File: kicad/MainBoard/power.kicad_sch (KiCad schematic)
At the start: 75 parts, among them J16 Conn_01x02_Female, J20 USB_C_Receptacle, Q16 AO3401A, Q17 AO3400A, SW1 SW_SPDT, U13 BQ27441-G1, U14 HY2111-GB, U15 FS8205A, U17 TPS61088, U2 BQ25601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

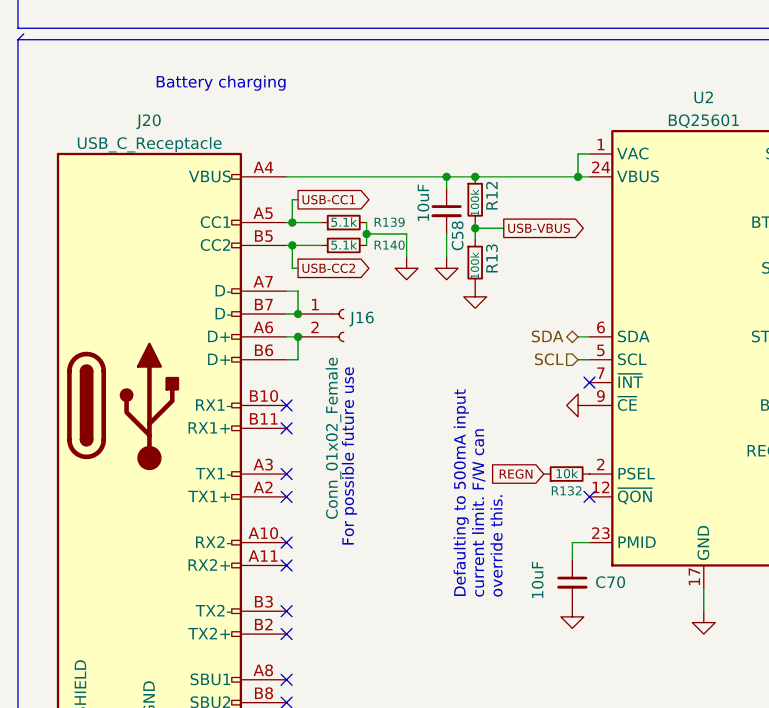
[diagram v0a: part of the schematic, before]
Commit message: v2.6 schematic + pcb changes
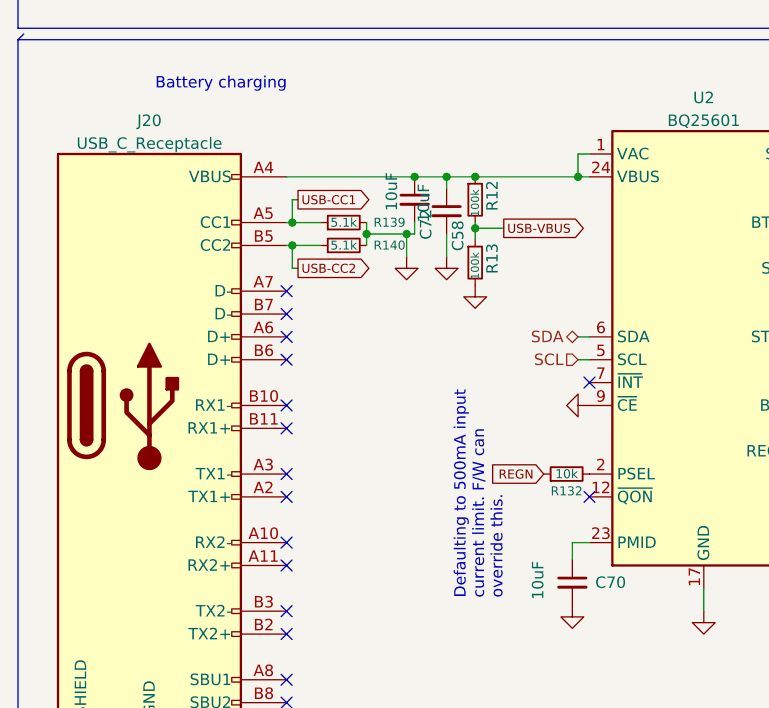
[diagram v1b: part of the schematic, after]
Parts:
- removed J16: Conn_01x02_Female, Connector_PinSocket_2.54mm:PinSocket_1x02_P2.54mm_Vertical, symbol Connector:Conn_01x02_Female
- added C72: 10uF, Capacitor_SMD:C_0603_1608Metric_Pad1.08x0.95mm_HandSolder, symbol Device:C_Small
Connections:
- net GND: now also C72.2
- net at J20.A7 (D-): no longer J20.B7 (D-)
- net at J20.A6 (D+): no longer J20.B6 (D+)
- net at C58.1, J20.A4 (VBUS), J20.A9 (VBUS)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: now also C72.1
- no-connect marks 14 -> 18
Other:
- note removed: "For possible future use"
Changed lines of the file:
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@@
   (junction (at 100.33 191.77) (diameter 0) (color 0 0 0 0)
   )
-  (junction (at 44.45 113.665) (diameter 0) (color 0 0 0 0)
-  )
   (junction (at 113.665 191.77) (diameter 0) (color 0 0 0 0)
   )
@@
   (junction (at 135.255 22.86) (diameter 0) (color 0 0 0 0)
   )
+  (junction (at 56.515 104.775) (diameter 0) (color 0 0 0 0)
+  )
   (junction (at 32.385 191.77) (diameter 0) (color 0 0 0 0)
   )
@@
   (junction (at 90.805 22.86) (diameter 0) (color 0 0 0 0)
   )
-  (junction (at 44.45 116.205) (diameter 0) (color 0 0 0 0)
-  )
   (junction (at 64.135 98.425) (diameter 0) (color 0 0 0 0)
   )
@@
   (junction (at 103.505 118.745) (diameter 0) (color 0 0 0 0)
   )
+  (junction (at 57.404 98.425) (diameter 0) (color 0 0 0 0)
+  )
   (junction (at 176.53 151.765) (diameter 0) (color 0 0 0 0)
   )
@@
   )
   (no_connect (at 43.18 149.225))
+  (no_connect (at 43.18 111.125))
   (no_connect (at 76.835 133.985))
   (no_connect (at 43.18 133.985))
   (no_connect (at 43.18 156.845))
+  (no_connect (at 43.18 116.205))
   (no_connect (at 43.18 131.445))
   (no_connect (at 43.18 139.065))
+  (no_connect (at 43.18 113.665))
   (no_connect (at 43.18 123.825))
   (no_connect (at 43.18 154.305))
+  (no_connect (at 43.18 118.745))
   (no_connect (at 76.835 121.285))
   (no_connect (at 43.18 126.365))
@@
     (stroke (width 0) (type default) (color 0 0 0 0))
   )
-  (wire (pts (xy 43.18 118.745) (xy 44.45 118.745))
-    (stroke (width 0) (type default) (color 0 0 0 0))
-  )
   (polyline (pts (xy 189.865 233.68) (xy 189.865 173.99))
     (stroke (width 0) (type default) (color 0 0 0 0))
@@
     (stroke (width 0) (type default) (color 0 0 0 0))
   )
-  (wire (pts (xy 43.18 116.205) (xy 44.45 116.205))
-    (stroke (width 0) (type default) (color 0 0 0 0))
-  )
   (wire (pts (xy 102.87 139.065) (xy 109.22 139.065))
     (stroke (width 0) (type default) (color 0 0 0 0))
@@
     (stroke (width 0) (type default) (color 0 0 0 0))
   )
+  (wire (pts (xy 57.404 103.505) (xy 57.404 104.775))
+    (stroke (width 0) (type default) (color 0 0 0 0))
+  )
   (wire (pts (xy 170.815 160.655) (xy 176.53 160.655))
     (stroke (width 0) (type default) (color 0 0 0 0))
@@
     (stroke (width 0) (type default) (color 0 0 0 0))
   )
+  (wire (pts (xy 52.07 104.775) (xy 56.515 104.775))
+    (stroke (width 0) (type default) (color 0 0 0 0))
+  )
   (wire (pts (xy 131.445 95.885) (xy 140.97 95.885))
     (stroke (width 0) (type default) (color 0 0 0 0))
@@
     (stroke (width 0) (type default) (color 0 0 0 0))
   )
-  (wire (pts (xy 44.45 111.125) (xy 44.45 113.665))
-    (stroke (width 0) (type default) (color 0 0 0 0))
-  )
   (wire (pts (xy 104.14 111.76) (xy 103.505 111.76))
     (stroke (width 0) (type default) (color 0 0 0 0))
   )
-  (wire (pts (xy 44.45 113.665) (xy 43.18 113.665))
-    (stroke (width 0) (type default) (color 0 0 0 0))
-  )
   (wire (pts (xy 114.3 95.885) (xy 116.84 95.885))
     (stroke (width 0) (type default) (color 0 0 0 0))
@@
     (stroke (width 0) (type default) (color 0 0 0 0))
   )
-  (wire (pts (xy 43.18 98.425) (xy 60.96 98.425))
+  (wire (pts (xy 43.18 98.425) (xy 57.404 98.425))
     (stroke (width 0) (type default) (color 0 0 0 0))
   )
@@
     (stroke (width 0) (type default) (color 0 0 0 0))
   )
-  (wire (pts (xy 43.18 111.125) (xy 44.45 111.125))
-    (stroke (width 0) (type default) (color 0 0 0 0))
-  )
   (polyline (pts (xy 13.335 172.085) (xy 13.335 83.185))
     (stroke (width 0) (type default) (color 0 0 0 0))
@@
     (stroke (width 0) (type default) (color 0 0 0 0))
   )
+  (wire (pts (xy 57.404 98.425) (xy 60.96 98.425))
+    (stroke (width 0) (type default) (color 0 0 0 0))
+  )
   (wire (pts (xy 90.17 191.77) (xy 90.17 192.405))
     (stroke (width 0) (type default) (color 0 0 0 0))
@@
     (stroke (width 0) (type default) (color 0 0 0 0))
   )
-  (wire (pts (xy 44.45 116.205) (xy 44.45 118.745))
-    (stroke (width 0) (type default) (color 0 0 0 0))
-  )
   (wire (pts (xy 58.42 208.28) (xy 45.72 208.28))
     (stroke (width 0) (type default) (color 0 0 0 0))
@@
     (stroke (width 0) (type default) (color 0 0 0 0))
   )
+  (wire (pts (xy 56.515 104.775) (xy 57.404 104.775))
+    (stroke (width 0) (type default) (color 0 0 0 0))
+  )
   (wire (pts (xy 41.91 191.77) (xy 41.91 203.2))
     (stroke (width 0) (type default) (color 0 0 0 0))
@@
   )
   (polyline (pts (xy 189.865 172.085) (xy 189.865 137.795))
-    (stroke (width 0) (type default) (color 0 0 0 0))
-  )
-  (wire (pts (xy 52.07 104.775) (xy 56.515 104.775))
     (stroke (width 0) (type default) (color 0 0 0 0))
   )
@@
   )
   (text "USB voltage sense" (at 25.4 242.57 0)
-    (effects (font (size 1.27 1.27)) (justify left bottom))
-  )
-  (text "For possible future use" (at 50.8 139.7 90)
     (effects (font (size 1.27 1.27)) (justify left bottom))
   )
@@
   (hierarchical_label "SW_SENSE1" (shape input) (at 31.75 265.43 180)
     (effects (font (size 1 1)) (justify right))
-  )
-  (symbol (lib_id "Connector:Conn_01x02_Female") (at 49.53 113.665 0) (unit 1)
-    (in_bom yes) (on_board yes)
-    (property "Reference" "J16" (id 0) (at 50.2412 114.1003 0)
-      (effects (font (size 1.27 1.27)) (justify left))
-    )
-    (property "Value" "Conn_01x02_Female" (id 1) (at 48.26 136.525 90)
-      (effects (font (size 1.27 1.27)) (justify left))
-    )
-    (property "Footprint" "Connector_PinSocket_2.54mm:PinSocket_1x02_P2.54mm_Vertical" (id 2) (at 49.53 113.665 0)
-      (effects (font (size 1.27 1.27)) hide)
-    )
-    (property "Datasheet" "~" (id 3) (at 49.53 113.665 0)
-      (effects (font (size 1.27 1.27)) hide)
-    )
-    (pin "1")
-    (pin "2")
   )
   (symbol (lib_id "Device:C_Small") (at 55.88 251.46 0) (unit 1)
@@
       (effects (font (size 1.27 1.27)) hide)
     )
+    (pin "1")
+    (pin "2")
+  )
+  (symbol (lib_id "Device:C_Small") (at 57.404 100.965 0) (unit 1)
+    (in_bom yes) (on_board yes)
+    (property "Reference" "C72" (id 0) (at 58.674 105.41 90)
+      (effects (font (size 1.27 1.27)) (justify left))
+    )
+    (property "Value" "10uF" (id 1) (at 54.864 102.235 90)
+      (effects (font (size 1.27 1.27)) (justify left))
+    )
+    (property "Footprint" "Capacitor_SMD:C_0603_1608Metric_Pad1.08x0.95mm_HandSolder" (id 2) (at 57.404 100.965 0)
+      (effects (font (size 1.27 1.27)) hide)
+    )
+    (property "Datasheet" "~" (id 3) (at 57.404 100.965 0)
+      (effects (font (size 1.27 1.27)) hide)
+    )
+    (property "LCSC" "C19702" (id 4) (at 57.404 100.965 0)
+      (effects (font (size 1.27 1.27)) hide)
+    )

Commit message: tweaks
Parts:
- C58: value 10uF -> DNP; LCSC C19702 -> (none)
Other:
- moved on the sheet: C58, C72, R12, R13
